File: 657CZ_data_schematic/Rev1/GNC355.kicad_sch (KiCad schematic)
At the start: 2 parts

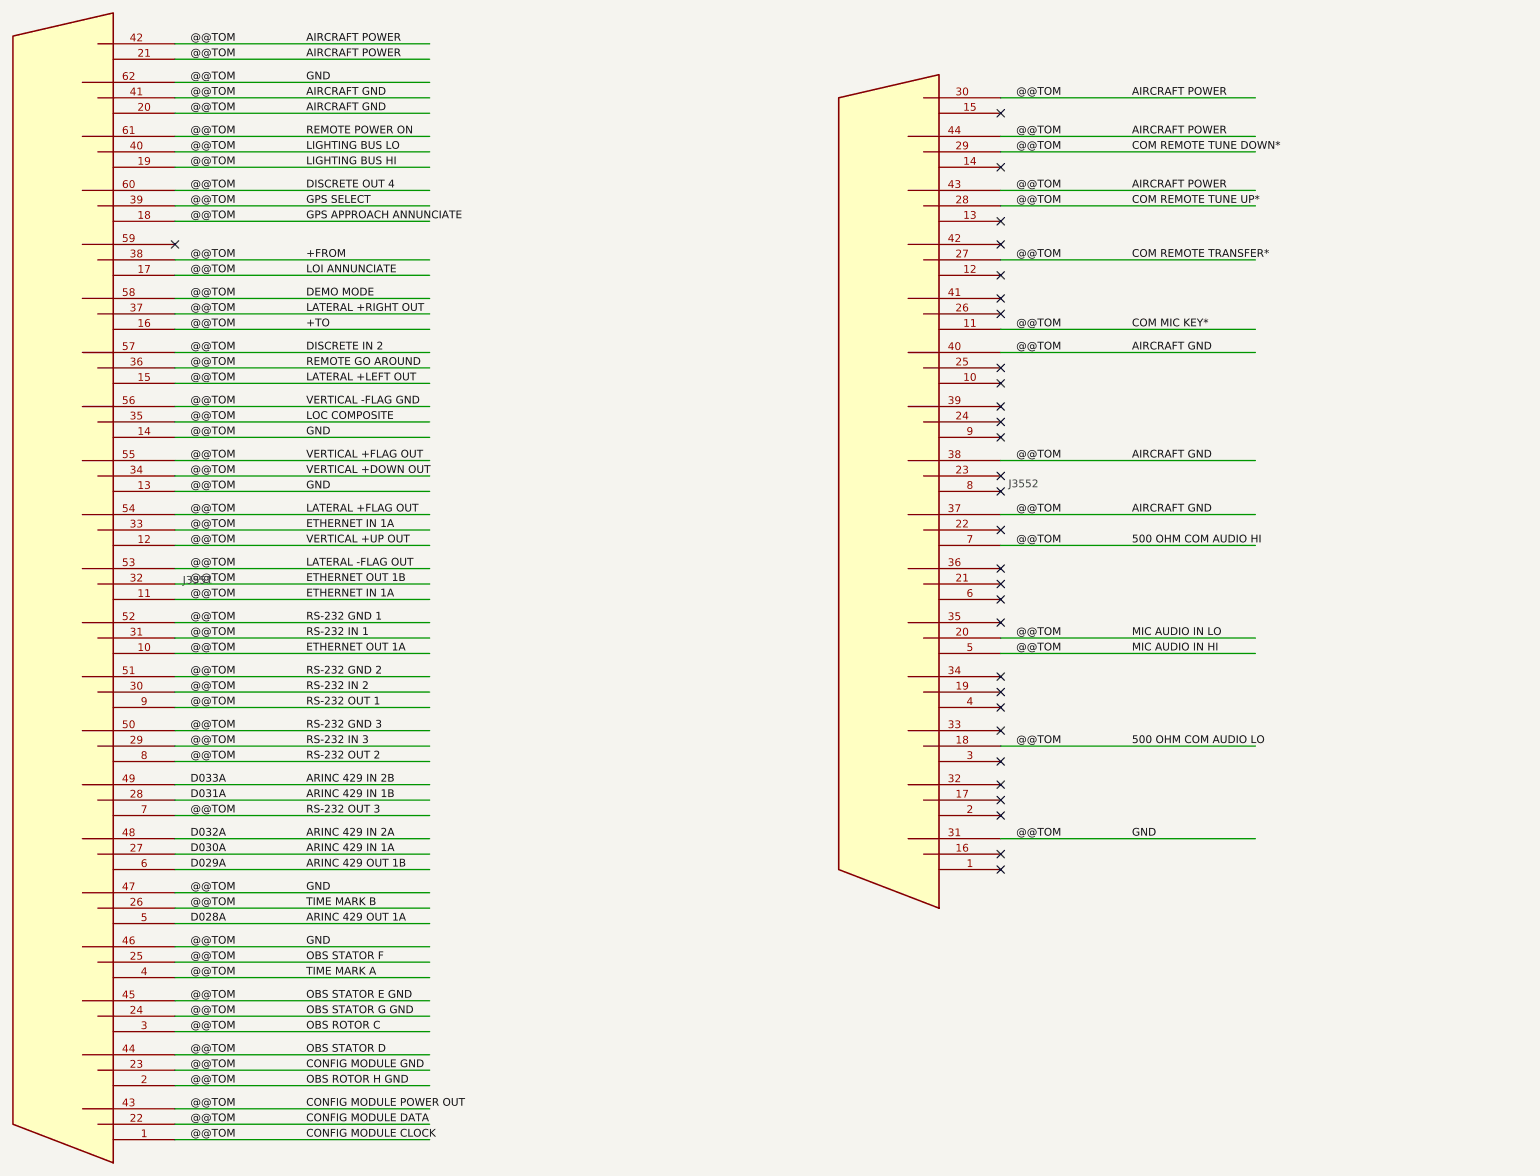
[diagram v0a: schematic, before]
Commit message: added data connections after AvClassics wiring. completed LRUs GMU, GDU, GSU, GAD, GNC, GTX, GTR  Not completed GMA, GEA and autopilot LRUs
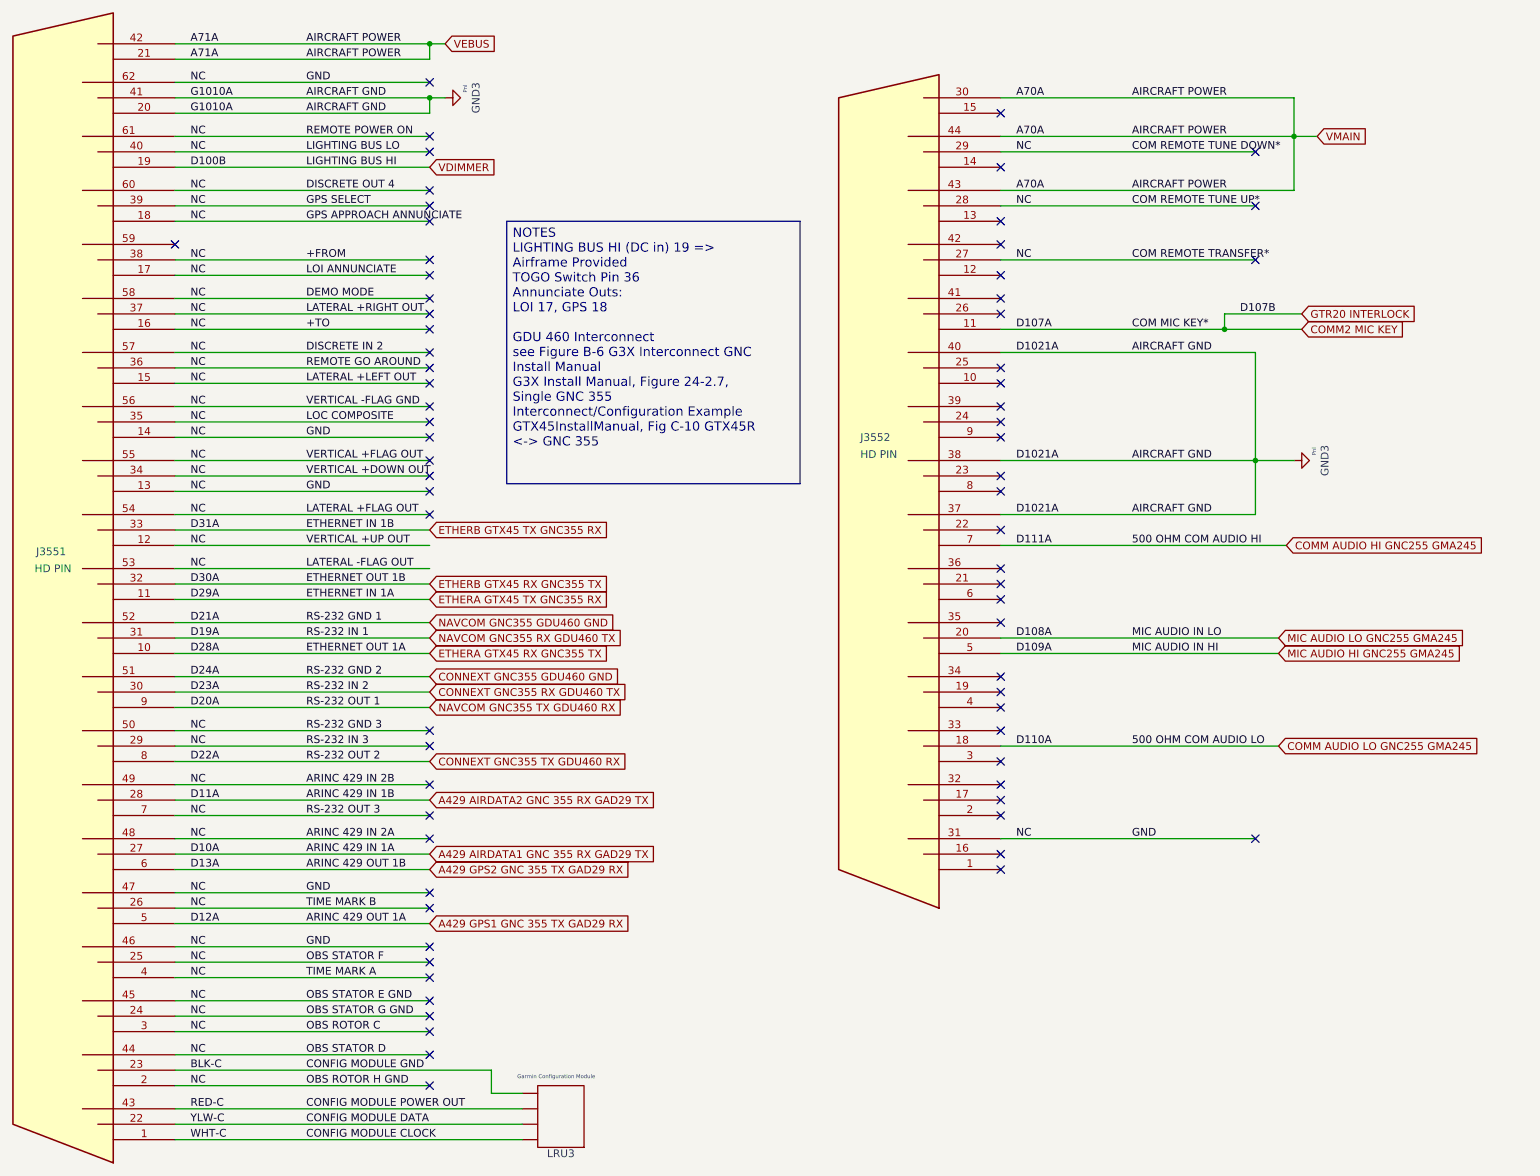
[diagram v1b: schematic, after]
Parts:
- added LRU3: ~, symbol AeroElectricConnectionSymbols:LRU_4x
- J3551, J3552: value ~ -> HD PIN
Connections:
- new net BLK-C: LRU3.1 (Red)
- new net CONFIG MODULE CLOCK: LRU3.4 (Blu)
- new net CONFIG MODULE DATA: LRU3.3 (Ylw)
- new net CONFIG MODULE POWER OUT: LRU3.2 (Blk)
- no-connect marks 30 -> 70
